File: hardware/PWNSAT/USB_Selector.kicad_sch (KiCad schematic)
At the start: 24 parts, among them J4 USB_A, J5 USB_A, SW4 USB Selector, U5 FSUSB30MUX, U6 MT3608, U7 AP2114H-3.3, U8 SL2.1A, Y3 Crystal_GND2

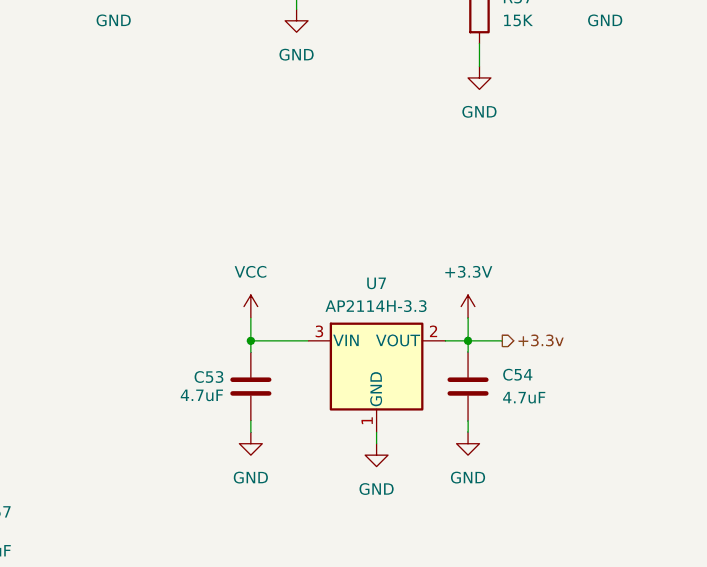
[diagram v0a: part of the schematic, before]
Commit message: feat(Hw):Update_Battery_Sch_And_Sensors_And_PWNCube
pending_Outputs_connectors
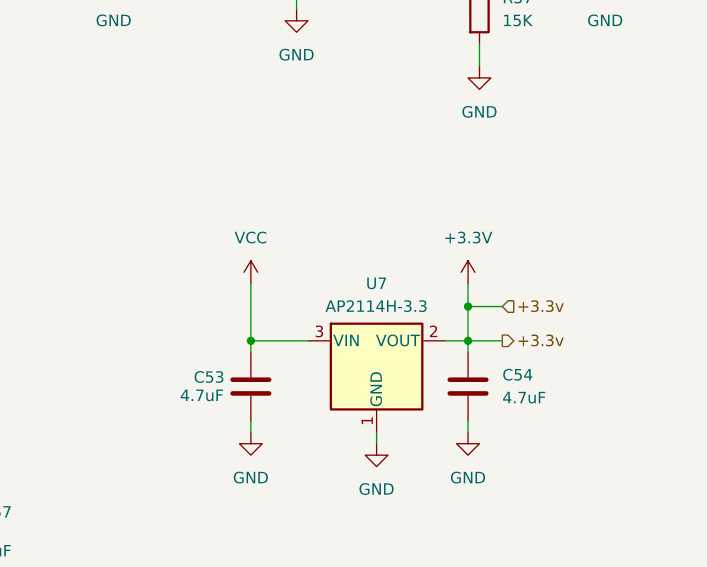
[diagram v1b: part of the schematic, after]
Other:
- company: (none) -> Electronic Cats
- title: (none) -> PWNCube
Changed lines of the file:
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@@
 	(generator_version "9.0")
 	(paper "A4")
+	(title_block
+		(title "PWNCube")
+		(date "2026-01-23")
+		(rev "1.0")
+		(company "Electronic Cats")
+		(comment 1 "Edgar Capuchino")
+	)
 	(text "HUB\n"
 		(exclude_from_sim no)
@@
 	)
 	(junction
+		(at 210.82 87.63)
+		(diameter 0)
+		(color 0 0 0 0)
+	)
+	(junction
 		(at 201.93 35.56)
 		(diameter 0)
@@
 	(wire
 		(pts
-			(xy 210.82 88.9) (xy 210.82 91.44)
+			(xy 210.82 85.09) (xy 210.82 87.63)
 		)
 		(stroke
@@
 	(wire
 		(pts
+			(xy 210.82 87.63) (xy 210.82 91.44)
+		)
+		(stroke
+			(width 0)
+			(type default)
+		)
+	)
+	(wire
+		(pts
 			(xy 78.74 57.15) (xy 78.74 55.88)
 		)
@@
 	(wire
 		(pts
-			(xy 186.69 88.9) (xy 186.69 91.44)
+			(xy 186.69 85.09) (xy 186.69 91.44)
 		)
 		(stroke
@@
 	(wire
 		(pts
+			(xy 210.82 87.63) (xy 214.63 87.63)
+		)
+		(stroke
+			(width 0)
+			(type default)
+		)
+	)
+	(wire
+		(pts
 			(xy 118.11 46.99) (xy 120.65 46.99)
 		)
@@
 	)
 	(hierarchical_label "+3.3v"
+		(shape input)
+		(at 214.63 87.63 0)
+		(effects
+			(font
+				(size 1.27 1.27)
+			)
+			(justify left)
+		)
+	)
+	(hierarchical_label "+3.3v"
 		(shape output)
 		(at 214.63 91.44 0)
@@
 	(symbol
 		(lib_id "power:VCC")
-		(at 186.69 88.9 0)
+		(at 186.69 85.09 0)
 		(unit 1)
 		(exclude_from_sim no)
@@
 		(fields_autoplaced yes)
 		(property "Reference" "#PWR0104"
-			(at 186.69 92.71 0)
+			(at 186.69 88.9 0)
 			(effects
 				(font
@@
 		)
 		(property "Value" "VCC"
-			(at 186.69 83.82 0)
+			(at 186.69 80.01 0)
 			(effects
 				(font
@@
 		)
 		(property "Footprint" ""
-			(at 186.69 88.9 0)
+			(at 186.69 85.09 0)
 			(effects
 				(font
@@
 		)
 		(property "Datasheet" ""
-			(at 186.69 88.9 0)
+			(at 186.69 85.09 0)
 			(effects
 				(font
@@
 		)
 		(property "Description" "Power symbol creates a global label with name \"VCC\""
-			(at 186.69 88.9 0)
+			(at 186.69 85.09 0)
 			(effects
 				(font
@@
 	(symbol
 		(lib_id "power:+3.3V")
-		(at 210.82 88.9 0)
+		(at 210.82 85.09 0)
 		(unit 1)
 		(exclude_from_sim no)
@@
 		(fields_autoplaced yes)
 		(property "Reference" "#PWR0105"
-			(at 210.82 92.71 0)
+			(at 210.82 88.9 0)
 			(effects
 				(font
@@
 		)
 		(property "Value" "+3.3V"
-			(at 210.82 83.82 0)
+			(at 210.82 80.01 0)
 			(effects
 				(font
@@
 		)
 		(property "Footprint" ""
-			(at 210.82 88.9 0)
+			(at 210.82 85.09 0)
 			(effects
 				(font
@@
 		)
 		(property "Datasheet" ""
-			(at 210.82 88.9 0)
+			(at 210.82 85.09 0)
 			(effects
 				(font
@@
 		)
 		(property "Description" "Power symbol creates a global label with name \"+3.3V\""
-			(at 210.82 88.9 0)
+			(at 210.82 85.09 0)
 			(effects
 				(font

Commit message: feat(Hw):floorplans_updated
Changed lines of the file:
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@@
-	)
-	(junction
-		(at 210.82 87.63)
-		(diameter 0)
-		(color 0 0 0 0)
 	)
 	(junction
@@
 	(wire
 		(pts
-			(xy 210.82 85.09) (xy 210.82 87.63)
+			(xy 210.82 85.09) (xy 210.82 91.44)
 		)
 		(stroke
@@
 	(wire
 		(pts
-			(xy 210.82 87.63) (xy 210.82 91.44)
-		)
-		(stroke
-			(width 0)
-			(type default)
-		)
-	)
-	(wire
-		(pts
 			(xy 78.74 57.15) (xy 78.74 55.88)
 		)
@@
 		(pts
 			(xy 201.93 43.18) (xy 199.39 43.18)
-		)
-		(stroke
-			(width 0)
-			(type default)
-		)
-	)
-	(wire
-		(pts
-			(xy 210.82 87.63) (xy 214.63 87.63)
 		)
 		(stroke
@@
 		)
 	)
-	(hierarchical_label "+3.3v"
-		(shape input)
-		(at 214.63 87.63 0)
-		(effects
-			(font
-				(size 1.27 1.27)
-			)
-			(justify left)
-		)
-	)

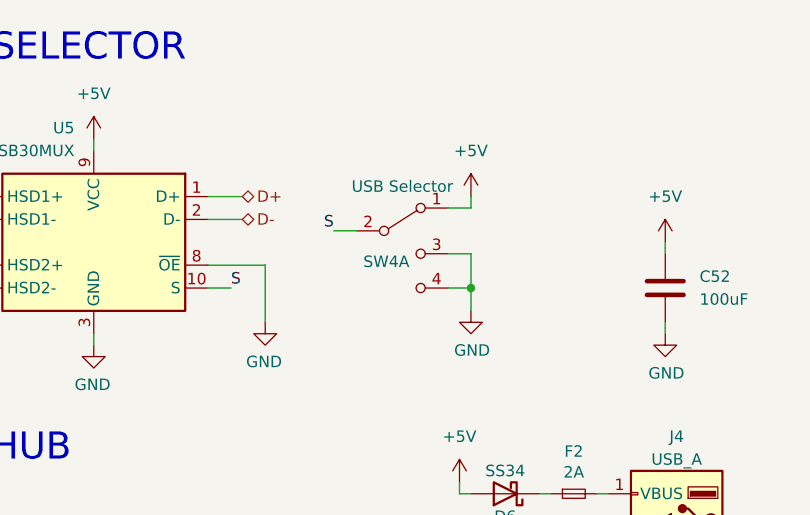
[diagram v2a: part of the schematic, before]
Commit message: feat(Hw):Route_UpdatedPWNcube_
Pending_3v3
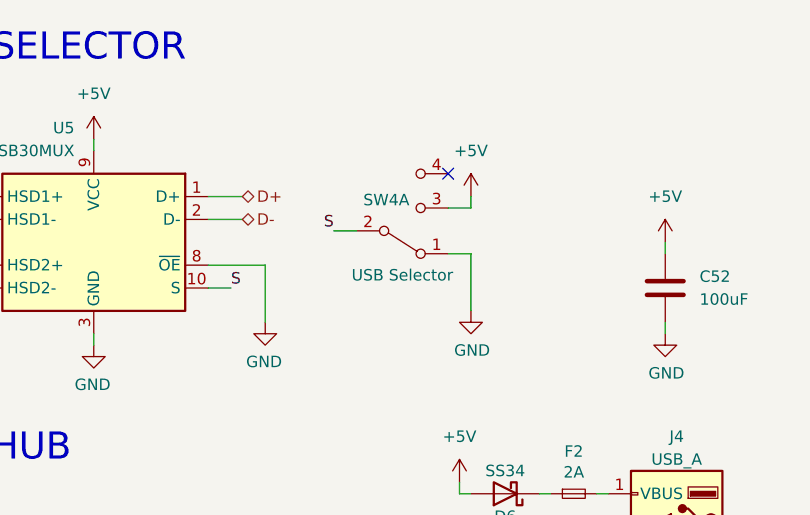
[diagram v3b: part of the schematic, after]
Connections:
- net +5V: now also SW4.3 (C); no longer SW4.1 (A)
- net GND: now also SW4.1 (A); no longer SW4.3 (C), SW4.4 (C)
- no-connect marks 4 -> 5
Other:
- moved on the sheet: SW4A
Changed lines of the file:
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@@
 	)
 	(junction
-		(at 120.65 50.8)
-		(diameter 0)
-		(color 0 0 0 0)
-	)
-	(junction
 		(at 212.09 35.56)
 		(diameter 0)
@@
 	)
 	(no_connect
+		(at 118.11 38.1)
+	)
+	(no_connect
 		(at 101.6 100.33)
 	)
@@
 	(wire
 		(pts
-			(xy 120.65 50.8) (xy 118.11 50.8)
-		)
-		(stroke
-			(width 0)
-			(type default)
-		)
-	)
-	(wire
-		(pts
 			(xy 144.78 123.19) (xy 146.05 123.19)
 		)
@@
 	(wire
 		(pts
-			(xy 120.65 53.34) (xy 120.65 50.8)
+			(xy 120.65 46.99) (xy 120.65 53.34)
 		)
 		(stroke
@@
 	(wire
 		(pts
-			(xy 120.65 46.99) (xy 120.65 50.8)
-		)
-		(stroke
-			(width 0)
-			(type default)
-		)
-	)
-	(wire
-		(pts
 			(xy 93.98 50.8) (xy 91.44 50.8)
 		)
@@
 		(lib_id "Switch:SW_DPDT_x2")
 		(at 113.03 44.45 0)
+		(mirror x)
 		(unit 1)
 		(exclude_from_sim no)
@@
 		(dnp no)
 		(property "Reference" "SW4"
-			(at 111.252 47.879 0)
+			(at 111.252 41.021 0)
 			(effects
 				(font
@@
 		)
 		(property "Value" "USB Selector"
-			(at 113.03 39.5224 0)
+			(at 113.03 49.3776 0)
 			(effects
 				(font
